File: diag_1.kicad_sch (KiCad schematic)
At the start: 36 parts, among them CN1 DRAGON-EDGE-CONN, IC1 29F040, IC2 32KSRAM-DIL600

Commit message: convert files to kicad, change to 4 layers and supplement decoupling
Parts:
- IC1, IC2: now left out of the parts list

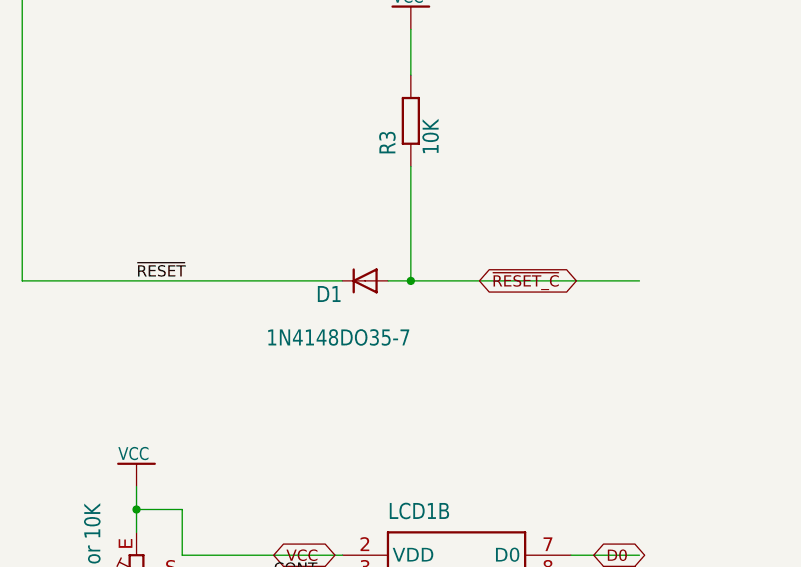
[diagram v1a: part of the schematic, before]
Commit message: convert more passives to smd
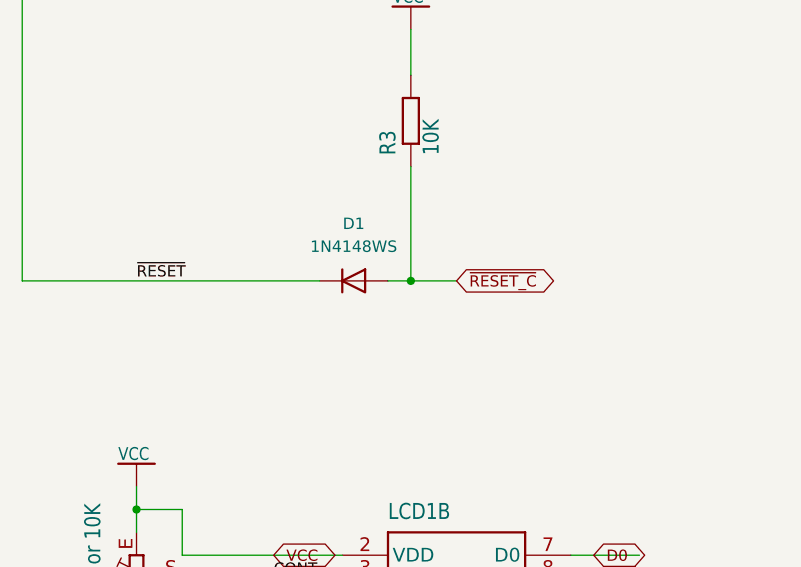
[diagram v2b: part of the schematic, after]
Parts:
- removed D1: 1N4148DO35-7, diag:DO35-7, symbol diag-eagle-import:1N4148DO35-7
- added D1: 1N4148WS, Diode_SMD:D_SOD-323, symbol Device:D
- R10, R11, R14, R2, R4, R5, R6, R7, R8, R9: footprint diag:0207_10 -> PCM_Resistor_SMD_AKL:R_0805_2012Metric
- R3: footprint diag:0204_7 -> PCM_Resistor_SMD_AKL:R_0805_2012Metric
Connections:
- net ~{RESET_C}: now also D1.2 (A)
- net ~{RESET}: now also D1.1 (K)
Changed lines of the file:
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@@
 	(wire
 		(pts
-			(xy 73.66 134.62) (xy 99.06 134.62)
+			(xy 73.66 134.62) (xy 78.74 134.62)
 		)
 		(stroke
@@
 		)
 	)
-	(wire
-		(pts
-			(xy 66.04 134.62) (xy 30.48 134.62)
-		)
-		(stroke
-			(width 0.1524)
-			(type solid)
-		)
-	)
 	(bus
 		(pts
@@
 	(wire
 		(pts
+			(xy 63.5 134.62) (xy 30.48 134.62)
+		)
+		(stroke
+			(width 0.1524)
+			(type solid)
+		)
+	)
+	(wire
+		(pts
 			(xy 297.18 203.2) (xy 297.18 208.28)
 		)
@@
 	(global_label "~{RESET_C}"
 		(shape bidirectional)
-		(at 81.28 134.62 0)
+		(at 78.74 134.62 0)
 		(fields_autoplaced yes)
 		(effects
@@
 		)
 		(property "Intersheetrefs" "${INTERSHEET_REFS}"
-			(at 93.1175 134.62 0)
+			(at 90.5775 134.62 0)
 			(effects
 				(font
@@
 			)
 		)
-		(property "Footprint" "diag:0207_10"
+		(property "Footprint" "PCM_Resistor_SMD_AKL:R_0805_2012Metric"
 			(at 378.46 137.16 0)
 			(effects
@@
 			)
 		)
-		(property "Footprint" "diag:0207_10"
+		(property "Footprint" "PCM_Resistor_SMD_AKL:R_0805_2012Metric"
 			(at 50.8 198.12 0)
 			(effects
@@
 			)
 		)
-		(property "Footprint" "diag:0204_7"
+		(property "Footprint" "PCM_Resistor_SMD_AKL:R_0805_2012Metric"
 			(at 73.66 116.84 0)
 			(effects
@@
 	)
 	(symbol
+		(lib_id "Device:D")
+		(at 67.31 134.62 0)
+		(unit 1)
+		(exclude_from_sim no)
+		(in_bom yes)
+		(on_board yes)
+		(dnp no)
+		(fields_autoplaced yes)
+		(property "Reference" "D1"
+			(at 67.31 128.27 0)
+			(effects
+				(font
+					(size 1.27 1.27)
+				)
+			)
+		)
+		(property "Value" "1N4148WS"
+			(at 67.31 130.81 0)
+			(effects
+				(font
+					(size 1.27 1.27)
+				)
+			)
+		)
+		(property "Footprint" "Diode_SMD:D_SOD-323"
+			(at 67.31 134.62 0)
+			(effects
+				(font
+					(size 1.27 1.27)
+				)
+				(hide yes)
+			)
+		)
+		(property "Datasheet" "~"
+			(at 67.31 134.62 0)
+			(effects
+				(font
+					(size 1.27 1.27)
+				)
+				(hide yes)
+			)
+		)
+		(property "Description" "Diode"
+			(at 67.31 134.62 0)
+			(effects
+				(font
+					(size 1.27 1.27)
+				)
+				(hide yes)
+			)
+		)
+		(property "Sim.Device" "D"
+			(at 67.31 134.62 0)
+			(effects
+				(font
+					(size 1.27 1.27)
+				)
+				(hide yes)
+			)
+		)
+		(property "Sim.Pins" "1=K 2=A"
+			(at 67.31 134.62 0)
+			(effects
+				(font
+					(size 1.27 1.27)
+				)
+				(hide yes)
+			)
+		)
+		(pin "1"
+		)
+		(pin "2"
+		)
+		(instances
+			(project "diag"
+				(path "/5591b95b-8e3f-4ee1-8f72-67906c158b98/498f4709-d0d2-49f7-b28c-fa2b7a9b8261"
+					(reference "D1")
+					(unit 1)
+				)
+			)
+		)
+	)
+	(symbol
 		(lib_id "diag-eagle-import:G10R")
 		(at 360.68 38.1 0)
@@
 			)
 		)
-		(property "Footprint" "diag:0207_10"
+		(property "Footprint" "PCM_Resistor_SMD_AKL:R_0805_2012Metric"
 			(at 129.54 45.72 0)
 			(effects
@@
 			)
 		)
-		(property "Footprint" "diag:0207_10"
+		(property "Footprint" "PCM_Resistor_SMD_AKL:R_0805_2012Metric"
 			(at 119.38 45.72 0)
 			(effects
@@
 			)
 		)
-		(property "Footprint" "diag:0207_10"
+		(property "Footprint" "PCM_Resistor_SMD_AKL:R_0805_2012Metric"
 			(at 137.16 109.22 0)
 			(effects
@@
 			)
 		)
-		(property "Footprint" "diag:0207_10"
+		(property "Footprint" "PCM_Resistor_SMD_AKL:R_0805_2012Metric"
 			(at 129.54 109.22 0)
 			(effects
@@
 	)
 	(symbol
-		(lib_id "diag-eagle-import:1N4148DO35-7")
-		(at 68.58 134.62 180)
-		(unit 1)
-		(exclude_from_sim no)
-		(in_bom yes)
-		(on_board yes)
-		(dnp no)
-		(property "Reference" "D1"
-			(at 66.04 135.1026 0)
-			(effects
-				(font
-					(size 1.778 1.5113)
-				)
-				(justify left bottom)
-			)
-		)
-		(property "Value" "1N4148DO35-7"
-			(at 73.66 139.9286 0)
-			(effects
-				(font
-					(size 1.778 1.5113)
-				)
-				(justify left bottom)
-			)
-		)
-		(property "Footprint" "diag:DO35-7"
-			(at 68.58 134.62 0)
-			(effects
-				(font
-					(size 1.27 1.27)
-				)
-				(hide yes)
-			)
-		)
-		(property "Datasheet" ""
-			(at 68.58 134.62 0)
-			(effects
-				(font
-					(size 1.27 1.27)
-				)
-				(hide yes)
-			)
-		)
-		(property "Description" ""
-			(at 68.58 134.62 0)
-			(effects
-				(font
-					(size 1.27 1.27)
-				)
-				(hide yes)
-			)
-		)
-		(pin "C"
-		)
-		(pin "A"
-		)
-		(instances
-			(project "diag"
-				(path "/5591b95b-8e3f-4ee1-8f72-67906c158b98/498f4709-d0d2-49f7-b28c-fa2b7a9b8261"
-					(reference "D1")
-					(unit 1)
-				)
-			)
-		)
-	)
-	(symbol
 		(lib_id "diag-eagle-import:VCC")
 		(at 43.18 195.58 0)
@@
 			)
 		)
-		(property "Footprint" "diag:0207_10"
+		(property "Footprint" "PCM_Resistor_SMD_AKL:R_0805_2012Metric"
 			(at 109.22 45.72 0)
 			(effects
@@
 			)
 		)
-		(property "Footprint" "diag:0207_10"
+		(property "Footprint" "PCM_Resistor_SMD_AKL:R_0805_2012Metric"
 			(at 121.92 109.22 0)
 			(effects
@@
 			)
 		)
-		(property "Footprint" "diag:0207_10"
+		(property "Footprint" "PCM_Resistor_SMD_AKL:R_0805_2012Metric"
 			(at 139.7 45.72 0)
 			(effects
@@
 			)
 		)
-		(property "Footprint" "diag:0207_10"
+		(property "Footprint" "PCM_Resistor_SMD_AKL:R_0805_2012Metric"
 			(at 129.54 226.06 0)
 			(effects

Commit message: tidy-up
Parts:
- C1, C2: footprint diag:C025-025X050 -> PCM_Capacitor_SMD_AKL:C_0805_2012Metric
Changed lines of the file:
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@@
 			)
 		)
-		(property "Footprint" "diag:C025-025X050"
+		(property "Footprint" "PCM_Capacitor_SMD_AKL:C_0805_2012Metric"
 			(at 383.54 213.36 0)
 			(effects
@@
 			)
 		)
-		(property "Footprint" "diag:C025-025X050"
+		(property "Footprint" "PCM_Capacitor_SMD_AKL:C_0805_2012Metric"
 			(at 373.38 213.36 0)
 			(effects
